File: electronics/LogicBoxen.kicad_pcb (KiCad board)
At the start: 2 copper layers, 0 parts

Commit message: Update schematics and board to latest version
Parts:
- added C1: C, Capacitors_SMD:C_0402, F.Cu at (36.0, 50.0)
- added K1: Power, Socket_Strips:Socket_Strip_Angled_1x03, F.Cu at (38.0, 32.3)
- added P1: Input, Socket_Strips:Socket_Strip_Angled_1x02, F.Cu at (25.8, 43.3)
- added P2: Output, Socket_Strips:Socket_Strip_Angled_1x02, F.Cu at (71.9, 48.3)
- added P3: CONN_01X05, Socket_Strips:Socket_Strip_Angled_1x05, F.Cu at (42.4, 61.5)
- added P4: CONN_01X05, Socket_Strips:Socket_Strip_Angled_1x05, F.Cu at (26.4, 61.5)
- added P5: CONN_01X06, Socket_Strips:Socket_Strip_Angled_1x06, F.Cu at (58.6, 61.5)
- added Q1: Q_NMOS_DGS, Housings_SOT-23_SOT-143_TSOT-6:SOT-23_Handsoldering, F.Cu at (48.6, 36.9)
- added R1: 220, Resistors_SMD:R_0402, B.Cu at (42.4, 59.0)
- added R10: 220, Resistors_SMD:R_0402, F.Cu at (66.2, 59.0)
- added R11: 220, Resistors_SMD:R_0402, F.Cu at (28.9, 59.0)
- added R12: 10k, Resistors_SMD:R_0402, F.Cu at (45.2, 44.0)
- added R13: 220, Resistors_SMD:R_0402, F.Cu at (68.8, 59.0)
- added R14: 220, Resistors_SMD:R_0402, B.Cu at (31.5, 59.0)
- added R15: 220, Resistors_SMD:R_0402, B.Cu at (34.0, 59.0)
- added R16: R, Resistors_SMD:R_0402, F.Cu at (50.2, 56.2)
- added R18: 10k, Resistors_SMD:R_0402, F.Cu at (67.0, 31.0)
- added R19: 10k, Resistors_SMD:R_0402, F.Cu at (64.5, 31.0)
- added R2: 220, Resistors_SMD:R_0402, B.Cu at (45.0, 59.0)
- added R20: 10k, Resistors_SMD:R_0402, F.Cu at (62.0, 31.0)
- added R21: 10k, Resistors_SMD:R_0402, F.Cu at (69.5, 31.0)
- added R22: 0R, Resistors_SMD:R_0402, F.Cu at (49.6, 34.6)
- added R3: 220, Resistors_SMD:R_0402, B.Cu at (47.5, 59.0)
- added R4: 220, Resistors_SMD:R_0402, B.Cu at (50.0, 59.0)
- added R5: 220, Resistors_SMD:R_0402, B.Cu at (58.5, 59.0)
- added R6: 10k, Resistors_SMD:R_0402, F.Cu at (34.8, 47.5)
- added R7: 220, Resistors_SMD:R_0402, F.Cu at (61.2, 59.0)
- added R8: 220, Resistors_SMD:R_0402, F.Cu at (63.8, 59.0)
- added R9: 220, Resistors_SMD:R_0402, F.Cu at (26.4, 59.0)
- added SW1: DIPS_04, Sockets_DIP:DIP-8__300, B.Cu at (65.8, 37.0)
- added U1: 4015, Housings_SSOP:TSSOP-16_4.4x5mm_Pitch0.65mm, F.Cu at (39.6, 45.5)
- added U2: 4050, Housings_SSOP:TSSOP-16_4.4x5mm_Pitch0.65mm, F.Cu at (55.8, 54.0)
- added U3: 4015, Housings_SSOP:TSSOP-16_4.4x5mm_Pitch0.65mm, F.Cu at (55.8, 45.8)
- added U4: 4050, Housings_SSOP:TSSOP-16_4.4x5mm_Pitch0.65mm, F.Cu at (39.6, 53.5)
- added U6: 4051, Housings_SSOP:TSSOP-16_4.4x5mm_Pitch0.65mm, F.Cu at (55.8, 37.0)
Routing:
- net VCC: track 0.00 -> 111.2 mm, vias 0 -> 6
- net /clock: track 0.00 -> 57.8 mm, vias 0 -> 3
- net /reset: track 0.00 -> 46.0 mm, vias 0 -> 4
- net /in_b: track 0.00 -> 38.3 mm, vias 0 -> 3
- net Net-(R9-Pad1): track 0.00 -> 34.1 mm, vias 0 -> 2
- net /in_a: track 0.00 -> 33.4 mm, vias 0 -> 3
- net Net-(R11-Pad1): track 0.00 -> 32.9 mm
- net Net-(Q1-Pad3): track 0.00 -> 29.8 mm, vias 0 -> 1
- net Net-(P2-Pad2): track 0.00 -> 27.1 mm
- net /out: track 0.00 -> 23.2 mm, vias 0 -> 2
- net Net-(U1-Pad13): track 0.00 -> 23.0 mm, vias 0 -> 3
- net Net-(U1-Pad12): track 0.00 -> 21.2 mm, vias 0 -> 2
- net Net-(P1-Pad1): track 0.00 -> 20.0 mm
- net Net-(U2-Pad9): track 0.00 -> 18.8 mm, vias 0 -> 2
- net Net-(R10-Pad1): track 0.00 -> 18.6 mm, vias 0 -> 2
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- added copper zone on F.Cu, net VSS
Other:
- board outline added: 50 x 35 mm
- net class Default: clearance 0.254 -> 0.2; trace_width 0.254 -> 0.25; via_dia 0.889 -> 0.6; via_drill 0.635 -> 0.4
- rule trace_clearance: 0.254 -> 0.2
- rule trace_min: 0.254 -> 0.2
- rule via_min_drill: 0.508 -> 0.3
- rule via_min_size: 0.889 -> 0.4

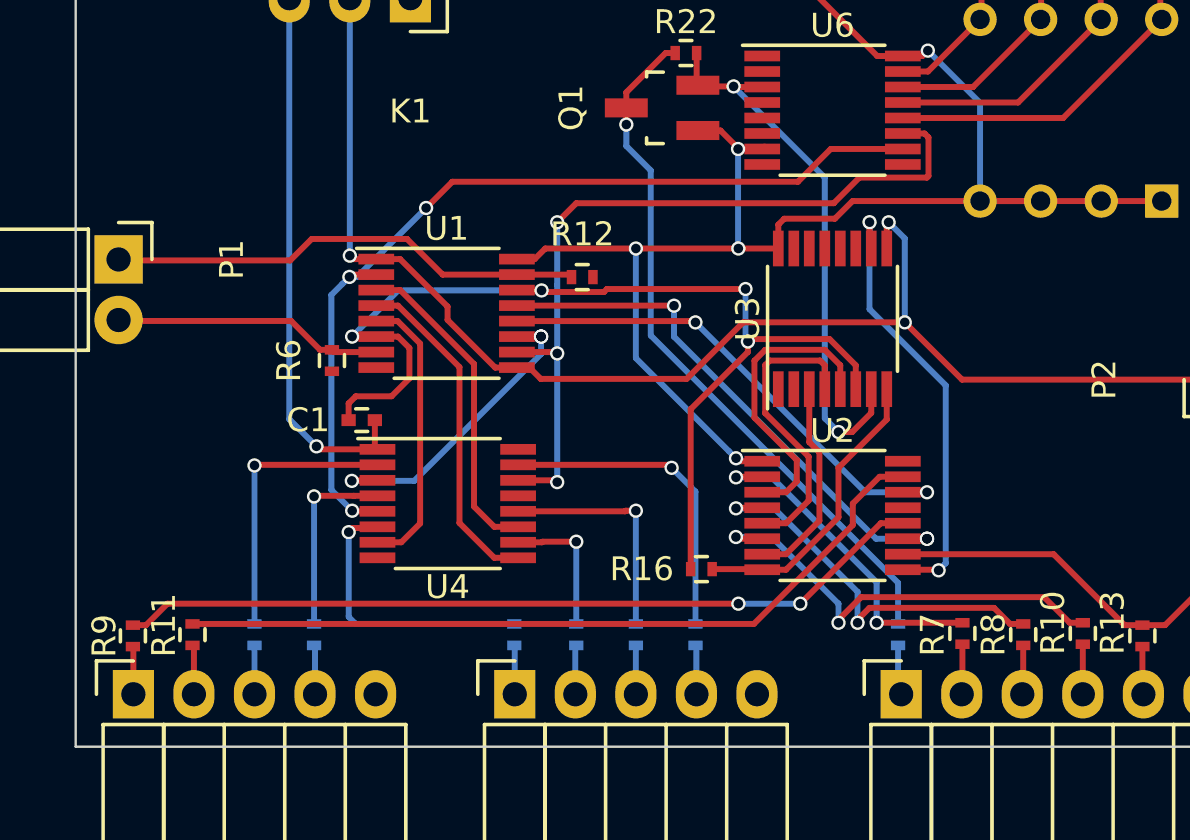
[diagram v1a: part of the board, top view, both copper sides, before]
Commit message: Move all resistors to same layer
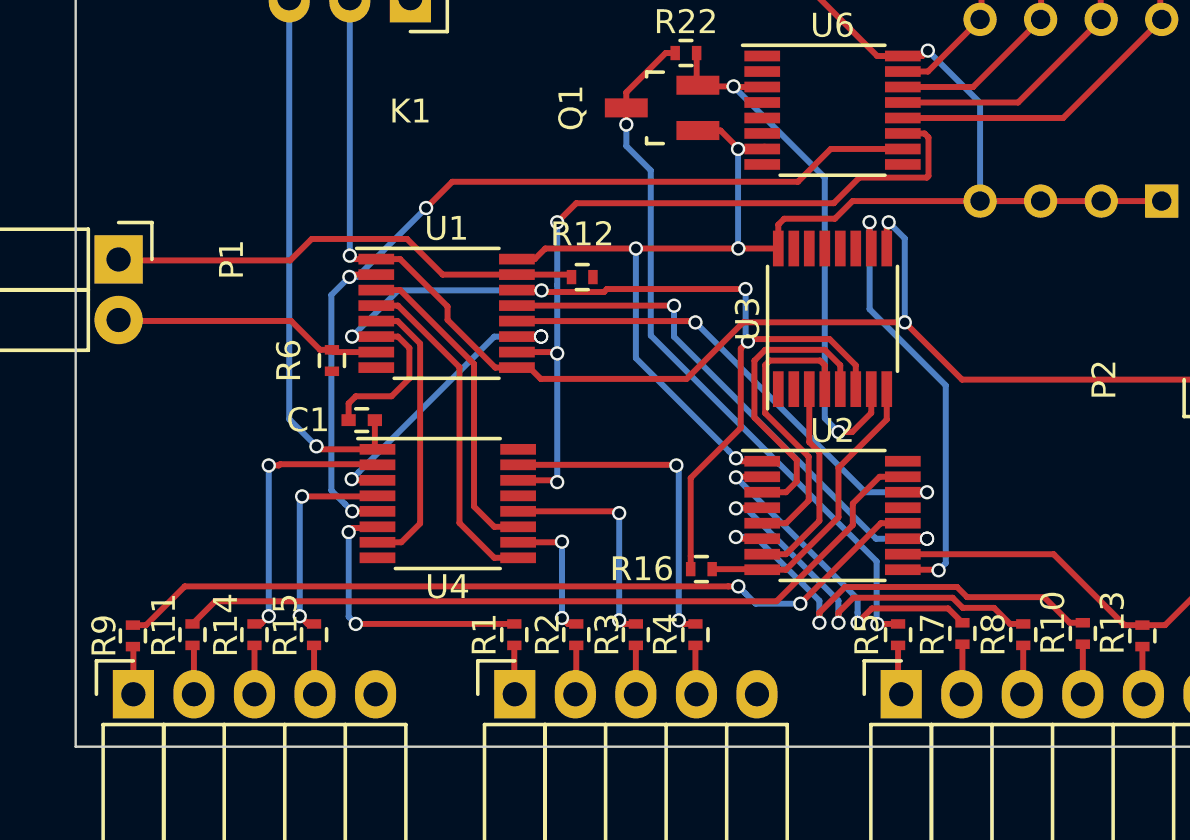
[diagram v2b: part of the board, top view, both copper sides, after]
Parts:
- R1, R14, R15, R2, R3, R4, R5: moved to F.Cu
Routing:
- net Net-(R15-Pad1): track 8.02 -> 8.97 mm, vias 1 -> 2
- net Net-(R9-Pad1): track 34.1 -> 34.7 mm
- net Net-(R10-Pad1): track 18.6 -> 19.2 mm
- net Net-(R4-Pad1): track 13.5 -> 14.0 mm, vias 1 -> 2
- net Net-(Q1-Pad3): track 29.8 -> 30.3 mm, vias 1 -> 2
- net Net-(R14-Pad1): track 11.8 -> 11.7 mm, vias 1 -> 2
- net Net-(R3-Pad1): track 9.70 -> 9.53 mm, vias 1 -> 2
- net Net-(R2-Pad1): track 5.90 -> 5.75 mm, vias 1 -> 2
- net Net-(R1-Pad1): vias 1 -> 2
